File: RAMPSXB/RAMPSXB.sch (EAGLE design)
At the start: 94 parts, among them CN1 1X4-BIG, CN2 1X4-BIG, CN3 1X4-BIG, CN4 1X4-BIG, CN5 1X4-BIG, CN6 1X4-BIG, CN7 1X4-BIG, CN8 1X4-BIG, CN9 1X4-BIG, J1 1X2-3.5MM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

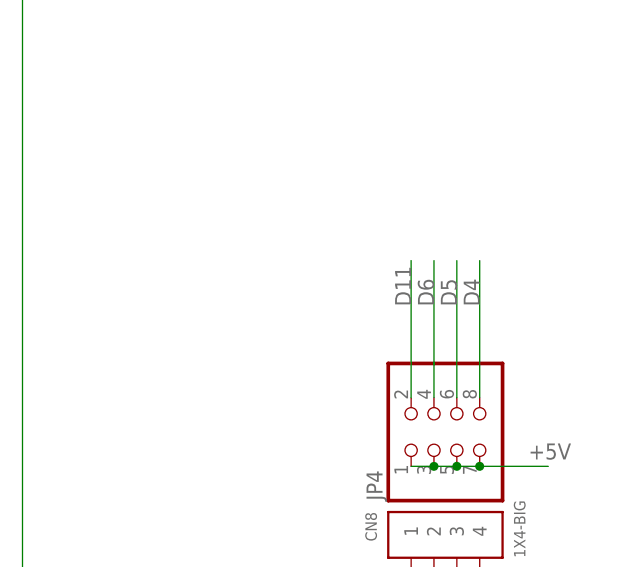
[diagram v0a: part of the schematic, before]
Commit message: Rerouting, broken out PWM pins
Rerouting, broken out PWM pins
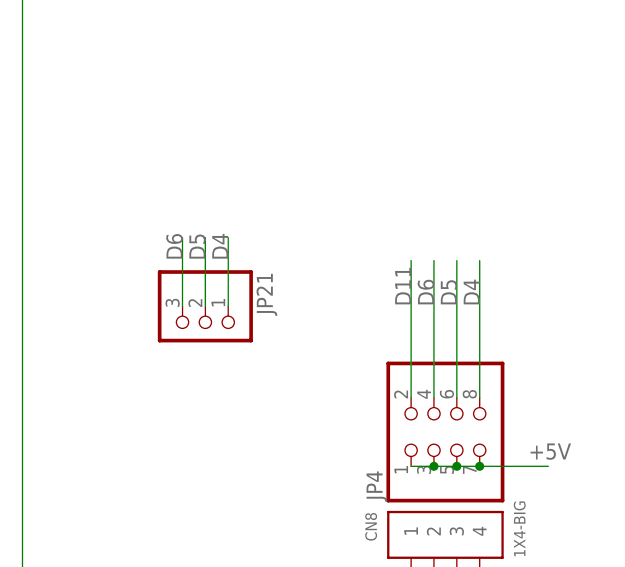
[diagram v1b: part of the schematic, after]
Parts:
- added JP21: (no value), adafruit:PINHD-1X3
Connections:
- net D4: now also JP21.1
- net D5: now also JP21.2
- net D6: now also JP21.3
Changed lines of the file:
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@@
 <?xml version="1.0" encoding="utf-8"?>
 <!DOCTYPE eagle SYSTEM "eagle.dtd">
-<eagle version="8.1.1">
+<eagle version="8.2.2">
 <drawing>
 <settings>
@@
 <part name="JP15" library="adafruit" deviceset="PINHD-2X4" device=""/>
 <part name="CN6" library="adafruit" deviceset="1X4" device="-BIG"/>
+<part name="JP21" library="adafruit" deviceset="PINHD-1X3" device=""/>
 </parts>
 <sheets>
@@
 <instance part="JP15" gate="A" x="63.5" y="-15.24"/>
 <instance part="CN6" gate="G$1" x="198.12" y="35.56" rot="R90"/>
+<instance part="JP21" gate="A" x="-58.42" y="-93.98" rot="R270"/>
 </instances>
 <busses>
@@
 <label x="327.66" y="-86.36" size="1.778" layer="95"/>
 </segment>
+<segment>
+<pinref part="JP21" gate="A" pin="3"/>
+<wire x1="-60.96" y1="-91.44" x2="-60.96" y2="-83.82" width="0.1524" layer="91"/>
+<label x="-60.96" y="-86.36" size="1.778" layer="95" rot="R90"/>
+</segment>
 </net>
 <net name="D5" class="0">
@@
 <label x="327.66" y="-104.14" size="1.778" layer="95"/>
 </segment>
+<segment>
+<pinref part="JP21" gate="A" pin="2"/>
+<wire x1="-58.42" y1="-91.44" x2="-58.42" y2="-83.82" width="0.1524" layer="91"/>
+<label x="-58.42" y="-86.36" size="1.778" layer="95" rot="R90"/>
+</segment>
 </net>
 <net name="D4" class="0">
@@
 <label x="327.66" y="-121.92" size="1.778" layer="95"/>
 </segment>
-</net>
+<segment>
+<pinref part="JP21" gate="A" pin="1"/>
+<wire x1="-55.88" y1="-91.44" x2="-55.88" y2="-83.82" width="0.1524" layer="91"/>
+<label x="-55.88" y="-86.36" size="1.778" layer="95" rot="R90"/>
+</segment>
+</net>

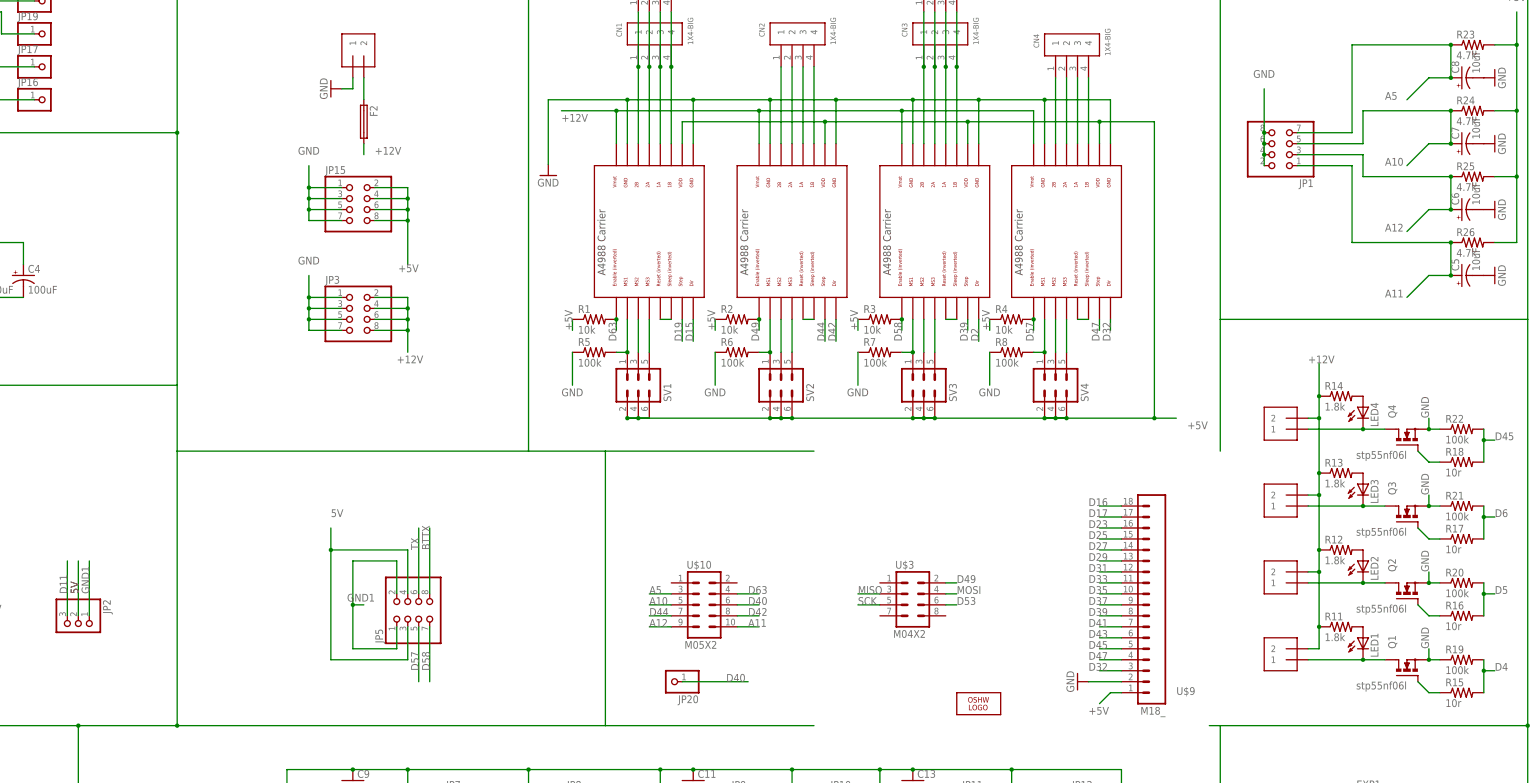
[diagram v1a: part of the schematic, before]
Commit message: Added Power Indicator and fixed a short.
Added Power indicator LED, and Fixed a major issue where +5V on the
arduino was connected to ground. Whoops.
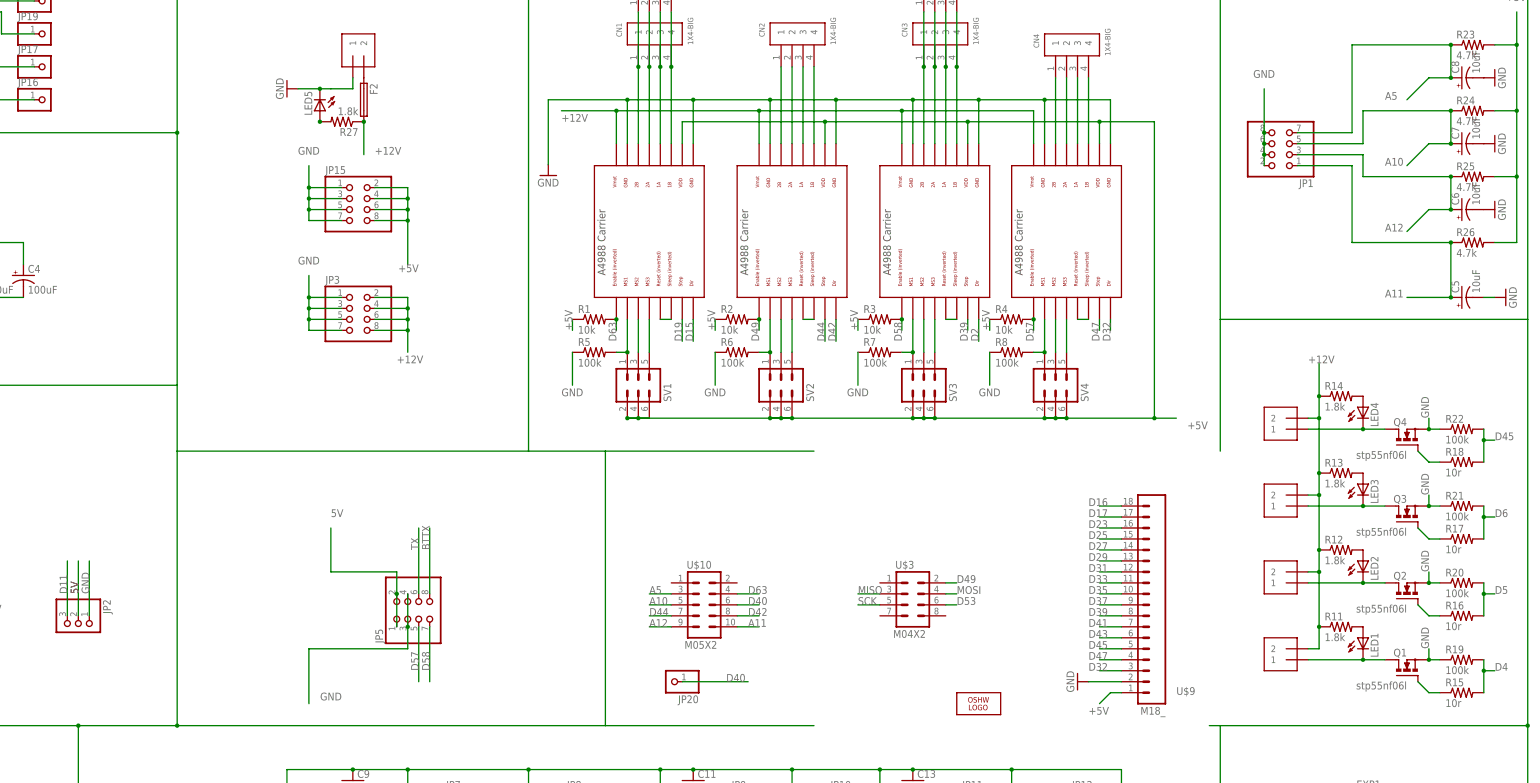
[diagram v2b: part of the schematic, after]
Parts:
- added LED5: (no value), adafruit:LEDCHIPLED_0805
- added R27: 1.8k, adafruit:R-US_M0805
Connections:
- new net N$2: LED5.A, R27.2
- net +12V: now also R27.1
- net 5V: now also JP5.1, JP5.2; no longer JP5.3, JP5.4
- net GND: now also JP2.1, JP5.3, JP5.4, LED5.C
- net GND1: no longer JP2.1, JP5.1, JP5.2
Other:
- moved on the sheet: C5, F2
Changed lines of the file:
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@@
 <part name="CN6" library="adafruit" deviceset="1X4" device="-BIG"/>
 <part name="JP21" library="adafruit" deviceset="PINHD-1X3" device=""/>
+<part name="R27" library="adafruit" deviceset="R-US_" device="M0805" value="1.8k"/>
+<part name="LED5" library="adafruit" deviceset="LED" device="CHIPLED_0805"/>
 </parts>
 <sheets>
@@
 <instance part="J1" gate="G$1" x="66.04" y="20.32" rot="R90"/>
 <instance part="GND1" gate="1" x="108.712" y="-7.366"/>
-<instance part="GND2" gate="1" x="58.42" y="12.7" rot="R270"/>
+<instance part="GND2" gate="1" x="48.26" y="12.7" rot="R270"/>
 <instance part="GND3" gate="1" x="231.14" y="-124.46" rot="R270"/>
 <instance part="C1" gate="G$1" x="-43.18" y="-30.48"/>
@@
 <instance part="J5" gate="G$1" x="279.4" y="-63.5" rot="R180"/>
 <instance part="Q1" gate="1" x="307.34" y="-121.92" smashed="yes" rot="R90">
-<attribute name="NAME" x="304.8" y="-116.84" size="1.778" layer="95" rot="R90"/>
+<attribute name="NAME" x="307.34" y="-116.84" size="1.778" layer="95" rot="R180"/>
 </instance>
 <instance part="Q2" gate="1" x="307.34" y="-104.14" smashed="yes" rot="R90">
-<attribute name="NAME" x="304.8" y="-99.06" size="1.778" layer="95" rot="R90"/>
+<attribute name="NAME" x="307.34" y="-99.06" size="1.778" layer="95" rot="R180"/>
 </instance>
 <instance part="Q3" gate="1" x="307.34" y="-86.36" smashed="yes" rot="R90">
-<attribute name="NAME" x="304.8" y="-81.28" size="1.778" layer="95" rot="R90"/>
+<attribute name="NAME" x="307.34" y="-81.28" size="1.778" layer="95" rot="R180"/>
 </instance>
 <instance part="Q4" gate="1" x="307.34" y="-68.58" smashed="yes" rot="R90">
-<attribute name="NAME" x="304.8" y="-63.5" size="1.778" layer="95" rot="R90"/>
+<attribute name="NAME" x="307.34" y="-63.5" size="1.778" layer="95" rot="R180"/>
 </instance>
 <instance part="LED1" gate="G$1" x="297.18" y="-114.3"/>
@@
 <instance part="R21" gate="G$1" x="320.04" y="-83.82"/>
 <instance part="R22" gate="G$1" x="320.04" y="-66.04"/>
-<instance part="C5" gate="G$1" x="320.04" y="-30.48" rot="R90"/>
+<instance part="C5" gate="G$1" x="320.04" y="-35.56" rot="R90"/>
 <instance part="C6" gate="G$1" x="320.04" y="-15.24" rot="R90"/>
 <instance part="C7" gate="G$1" x="320.04" y="0" rot="R90"/>
@@
 <instance part="GND10" gate="1" x="327.66" y="0" rot="R90"/>
 <instance part="GND11" gate="1" x="327.66" y="-15.24" rot="R90"/>
-<instance part="GND12" gate="1" x="327.66" y="-30.48" rot="R90"/>
+<instance part="GND12" gate="1" x="330.2" y="-35.56" rot="R90"/>
 <instance part="JP1" gate="A" x="279.4" y="0" rot="R180"/>
 <instance part="JP3" gate="A" x="63.5" y="-40.64"/>
@@
 <instance part="R9" gate="G$1" x="-53.34" y="-162.56" rot="R90"/>
 <instance part="R10" gate="G$1" x="-53.34" y="-175.26" rot="R90"/>
-<instance part="F2" gate="A" x="66.04" y="5.08" rot="R270"/>
+<instance part="F2" gate="A" x="66.04" y="10.16" rot="R270"/>
 <instance part="JP2" gate="A" x="0" y="-111.76" rot="R270"/>
 <instance part="JP16" gate="G$1" x="-7.62" y="10.16"/>
@@
 <instance part="CN6" gate="G$1" x="198.12" y="35.56" rot="R90"/>
 <instance part="JP21" gate="A" x="-58.42" y="-93.98" rot="R270"/>
+<instance part="R27" gate="G$1" x="60.96" y="5.08" rot="R180"/>
+<instance part="LED5" gate="G$1" x="55.88" y="7.62" rot="R180"/>
 </instances>
 <busses>
@@
 <pinref part="GND2" gate="1" pin="GND"/>
 <pinref part="J1" gate="G$1" pin="1"/>
-<wire x1="60.96" y1="12.7" x2="63.5" y2="12.7" width="0.1524" layer="91"/>
+<wire x1="50.8" y1="12.7" x2="55.88" y2="12.7" width="0.1524" layer="91"/>
+<wire x1="58.42" y1="12.7" x2="63.5" y2="12.7" width="0.1524" layer="91"/>
 <wire x1="63.5" y1="12.7" x2="63.5" y2="15.24" width="0.1524" layer="91"/>
+<pinref part="LED5" gate="G$1" pin="C"/>
+<wire x1="58.42" y1="12.7" x2="55.88" y2="12.7" width="0.1524" layer="91"/>
+<junction x="55.88" y="12.7"/>
 </segment>
 <segment>
@@
 <pinref part="GND12" gate="1" pin="GND"/>
 <pinref part="C5" gate="G$1" pin="-"/>
+<wire x1="325.12" y1="-35.56" x2="327.66" y2="-35.56" width="0.1524" layer="91"/>
 </segment>
 <segment>
@@
 <label x="-38.1" y="27.94" size="1.778" layer="95"/>
 </segment>
+<segment>
+<label x="60.96" y="-127" size="1.778" layer="95" rot="R180"/>
+<wire x1="53.34" y1="-116.84" x2="53.34" y2="-129.54" width="0.1524" layer="91"/>
+<pinref part="JP5" gate="A" pin="3"/>
+<pinref part="JP5" gate="A" pin="4"/>
+<wire x1="76.2" y1="-111.76" x2="76.2" y2="-104.14" width="0.1524" layer="91"/>
+<wire x1="76.2" y1="-111.76" x2="76.2" y2="-116.84" width="0.1524" layer="91"/>
+<junction x="76.2" y="-111.76"/>
+<wire x1="76.2" y1="-116.84" x2="53.34" y2="-116.84" width="0.1524" layer="91"/>
+</segment>
+<segment>
+<pinref part="JP2" gate="A" pin="1"/>
+<wire x1="2.54" y1="-109.22" x2="2.54" y2="-96.52" width="0.1524" layer="91"/>
+<label x="2.54" y="-104.14" size="1.778" layer="95" rot="R90"/>
+</segment>
 </net>
 <net name="N$17" class="0">
 <segment>
 <pinref part="J1" gate="G$1" pin="2"/>
-<wire x1="66.04" y1="15.24" x2="66.04" y2="10.16" width="0.1524" layer="91"/>
 <pinref part="F2" gate="A" pin="1"/>
 </segment>
@@
 <net name="+12V" class="0">
 <segment>
-<wire x1="66.04" y1="0" x2="66.04" y2="-2.54" width="0.1524" layer="91"/>
+<wire x1="66.04" y1="5.08" x2="66.04" y2="-2.54" width="0.1524" layer="91"/>
 <label x="68.58" y="-2.54" size="1.778" layer="95"/>
 <pinref part="F2" gate="A" pin="2"/>
+<pinref part="R27" gate="G$1" pin="1"/>
+<junction x="66.04" y="5.08"/>
 </segment>
 <segment>
@@
 <pinref part="R26" gate="G$1" pin="1"/>
 <pinref part="C5" gate="G$1" pin="+"/>
-<wire x1="317.5" y1="-22.86" x2="317.5" y2="-30.48" width="0.1524" layer="91"/>
-<wire x1="317.5" y1="-30.48" x2="312.42" y2="-30.48" width="0.1524" layer="91"/>
-<wire x1="312.42" y1="-30.48" x2="307.34" y2="-35.56" width="0.1524" layer="91"/>
-<junction x="317.5" y="-30.48"/>
+<wire x1="317.5" y1="-22.86" x2="317.5" y2="-35.56" width="0.1524" layer="91"/>
+<wire x1="317.5" y1="-35.56" x2="307.34" y2="-35.56" width="0.1524" layer="91"/>
+<junction x="317.5" y="-35.56"/>
 <wire x1="317.5" y1="-22.86" x2="294.64" y2="-22.86" width="0.1524" layer="91"/>
 <junction x="317.5" y="-22.86"/>
@@
 <net name="GND1" class="0">
 <segment>
-<pinref part="JP5" gate="A" pin="2"/>
-<wire x1="73.66" y1="-104.14" x2="73.66" y2="-96.52" width="0.1524" layer="91"/>
-<wire x1="73.66" y1="-96.52" x2="63.5" y2="-96.52" width="0.1524" layer="91"/>
-<wire x1="63.5" y1="-96.52" x2="63.5" y2="-106.68" width="0.1524" layer="91"/>
-<pinref part="JP5" gate="A" pin="1"/>
-<wire x1="63.5" y1="-106.68" x2="63.5" y2="-116.84" width="0.1524" layer="91"/>
-<wire x1="63.5" y1="-116.84" x2="73.66" y2="-116.84" width="0.1524" layer="91"/>
-<wire x1="73.66" y1="-116.84" x2="73.66" y2="-111.76" width="0.1524" layer="91"/>
-<wire x1="63.5" y1="-106.68" x2="66.04" y2="-106.68" width="0.1524" layer="91"/>
-<junction x="63.5" y="-106.68"/>
-<label x="68.58" y="-104.14" size="1.778" layer="95" rot="R180"/>
-</segment>
-<segment>
 <pinref part="R10" gate="G$1" pin="1"/>
 <wire x1="-53.34" y1="-180.34" x2="-53.34" y2="-182.88" width="0.1524" layer="91"/>
 <label x="-55.88" y="-187.96" size="1.778" layer="95"/>
 </segment>
-<segment>
-<pinref part="JP2" gate="A" pin="1"/>
-<wire x1="2.54" y1="-109.22" x2="2.54" y2="-96.52" width="0.1524" layer="91"/>
-<label x="2.54" y="-104.14" size="1.778" layer="95" rot="R90"/>
-</segment>
 </net>
 <net name="5V" class="0">
 <segment>
-<pinref part="JP5" gate="A" pin="3"/>
-<wire x1="76.2" y1="-111.76" x2="76.2" y2="-119.38" width="0.1524" layer="91"/>
-<wire x1="76.2" y1="-119.38" x2="58.42" y2="-119.38" width="0.1524" layer="91"/>
-<wire x1="58.42" y1="-119.38" x2="58.42" y2="-93.98" width="0.1524" layer="91"/>
-<wire x1="58.42" y1="-93.98" x2="76.2" y2="-93.98" width="0.1524" layer="91"/>
-<pinref part="JP5" gate="A" pin="4"/>
-<wire x1="76.2" y1="-93.98" x2="76.2" y2="-104.14" width="0.1524" layer="91"/>
-<wire x1="58.42" y1="-93.98" x2="58.42" y2="-88.9" width="0.1524" layer="91"/>
-<junction x="58.42" y="-93.98"/>
+<wire x1="58.42" y1="-99.06" x2="58.42" y2="-88.9" width="0.1524" layer="91"/>
 <label x="58.42" y="-86.36" size="1.778" layer="95"/>
+<pinref part="JP5" gate="A" pin="2"/>
+<wire x1="58.42" y1="-99.06" x2="73.66" y2="-99.06" width="0.1524" layer="91"/>
+<wire x1="73.66" y1="-99.06" x2="73.66" y2="-104.14" width="0.1524" layer="91"/>
+<pinref part="JP5" gate="A" pin="1"/>
+<wire x1="73.66" y1="-104.14" x2="73.66" y2="-111.76" width="0.1524" layer="91"/>
+<junction x="73.66" y="-104.14"/>
 </segment>
 <segment>
@@
 </segment>
 </net>
+<net name="N$2" class="0">
+<segment>
+<pinref part="R27" gate="G$1" pin="2"/>
+<pinref part="LED5" gate="G$1" pin="A"/>
+<junction x="55.88" y="5.08"/>
+</segment>
+</net>

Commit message: Added Gerber Files. Slight Rewiring.
Added Gerber Files for production run. Fixed some clearance issues.
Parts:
- removed C13: 0.47uF, adafruit:C-USC0805
- added C10: 0.47uF, adafruit:C-USC0805
- renumbered F2 to F1
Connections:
- net D14: now also C10.2; no longer C11.2
- net D18: now also C11.2; no longer C13.2
- net GND: now also C10.1; no longer C13.1
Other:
- note added: "RAMPSXB"
- note added: "http://reprap.org/wiki/RAMPSXB"
- moved on the sheet: C11, C6, C8, R23, R24, R26
